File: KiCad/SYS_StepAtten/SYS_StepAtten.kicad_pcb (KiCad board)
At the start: 2 copper layers, 122 x 84 mm, 143 parts, among them J1 RCA-Out, J10 A/D GND Jumper, J11 ADJ_L, J12 ADJ_R, J2 RCA-1, J3 RCA-2, J4 AUX-1-2, J5 Barrel_Jack 9Vdc, J6 POT_EXT Conn, J7 cfg jumper, J8 ARM SWD, J9 A/D GND Jumper, K1 TQ2SA, K10 TQ2SA, K11 TQ2SA, K12 TQ2SA, K13 TQ2SA, K14 TQ2SA, K2 TQ2SA, K3 TQ2SA, K4 TQ2SA, K5 TQ2SA, K6 TQ2SA, K7 TQ2SA, K8 TQ2SA, K9 TQ2SA, Q1 2N7002, Q10 2N7002, Q11 2N7002, Q12 2N7002, Q13 2N7002, Q14 2N7002, Q2 2N7002, Q3 2N7002, Q4 2N7002, Q5 2N7002, Q6 2N7002, Q7 2N7002, Q8 2N7002, Q9 2N7002, SW1 INPUT_SWITCH, SW2 ON/OFF, U1 LM317, U2 MC34063AD, U4 STM32f030K6T6

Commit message: Updated PCB
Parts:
- removed REF**: KiCad-Logo2_5mm_SilkScreen, Symbol:KiCad-Logo2_5mm_SilkScreen

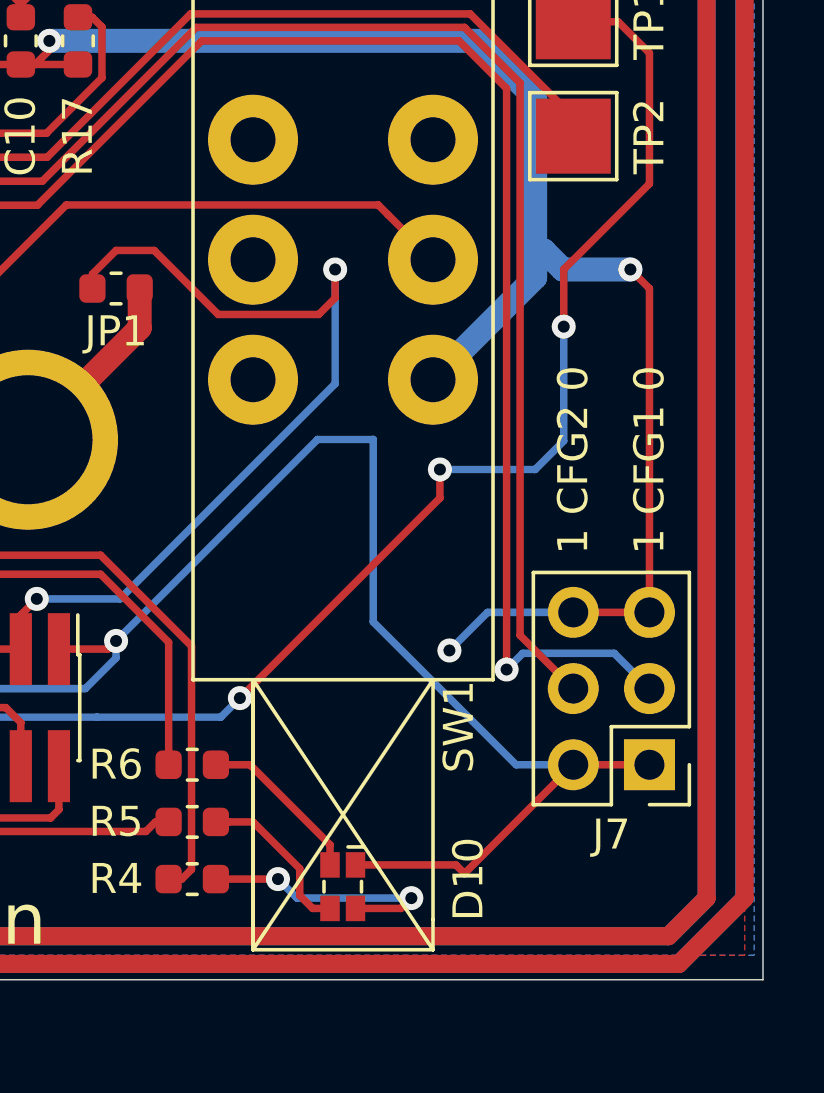
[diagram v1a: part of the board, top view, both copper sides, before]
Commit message: Added Pulldowns to configuration jumpers
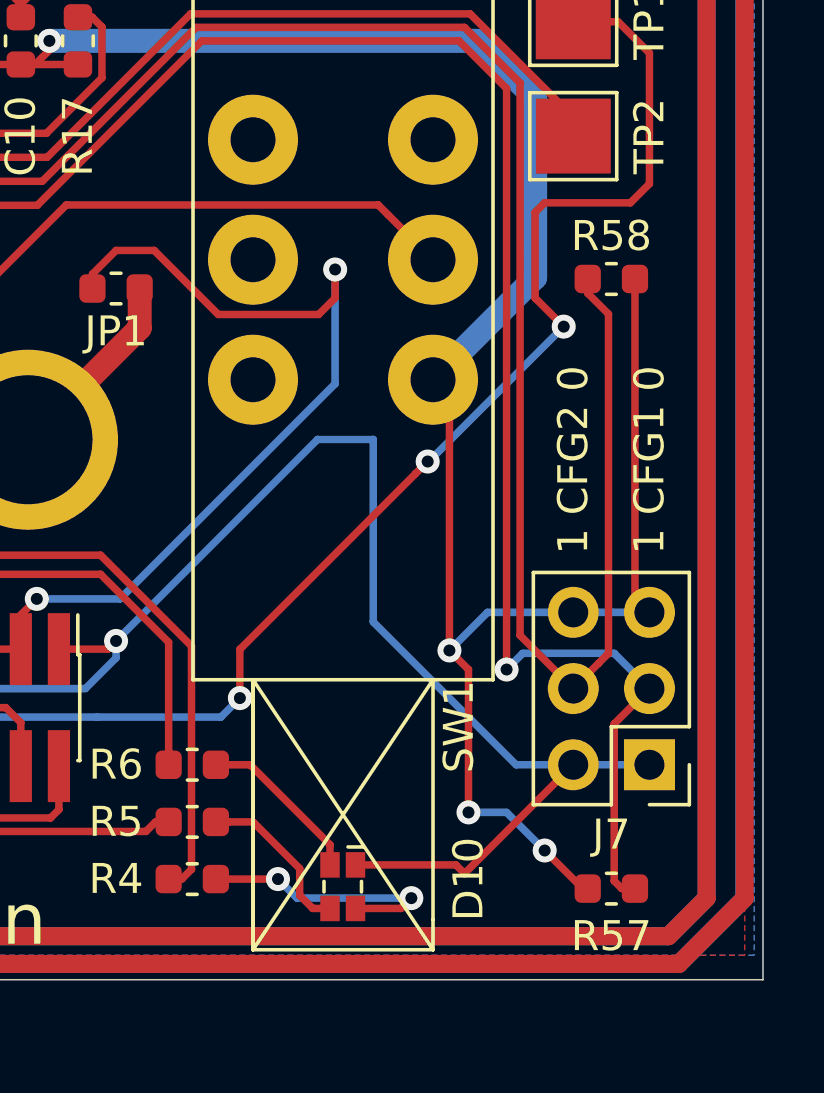
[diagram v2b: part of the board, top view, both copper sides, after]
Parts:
- added R57: 10K, Resistor_SMD:R_0603_1608Metric, F.Cu at (194.9, 144.5)
- added R58: 10K, Resistor_SMD:R_0603_1608Metric, F.Cu at (194.9, 124.1)
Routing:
- net GND: track 529.8 -> 544.6 mm, vias 32 -> 33
- net /cfg2: track 47.1 -> 61.5 mm
- net /cfg1: track 50.6 -> 58.3 mm
- net /NRST: track 79.1 -> 79.7 mm

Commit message: Updated Layout.
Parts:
- added F2: 0.15A, Fuse:Fuse_1206_3216Metric, F.Cu at (135.9, 76.2)
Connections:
- J6 pad 3: +3V3 -> Net-(F2-Pad1)
- U4 pad 14: /led0 -> /extctrl_pot
- U4 pad 27: /extctrl_pot -> /led0
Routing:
- net /led0: track 44.8 -> 34.9 mm, vias 4 -> 2
- net /extctrl_pot: track 21.5 -> 12.0 mm
- net Net-(F2-Pad1): track 0.00 -> 6.93 mm
- net +3V3: track 211.2 -> 209.6 mm
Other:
- board text added: "v1.3"
- board text removed: "v1.1"
